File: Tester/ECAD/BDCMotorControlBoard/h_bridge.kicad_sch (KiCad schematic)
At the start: 58 parts, among them Q2 IRLR8726, Q3 IRLR8726, Q4 IRLR8726, Q5 IRLR8726, Q6 BC846, Q7 BC846BPN, Q8 BC846, Q9 BC846, U4 IR2103, U5 INA180A2, U6 IR2103

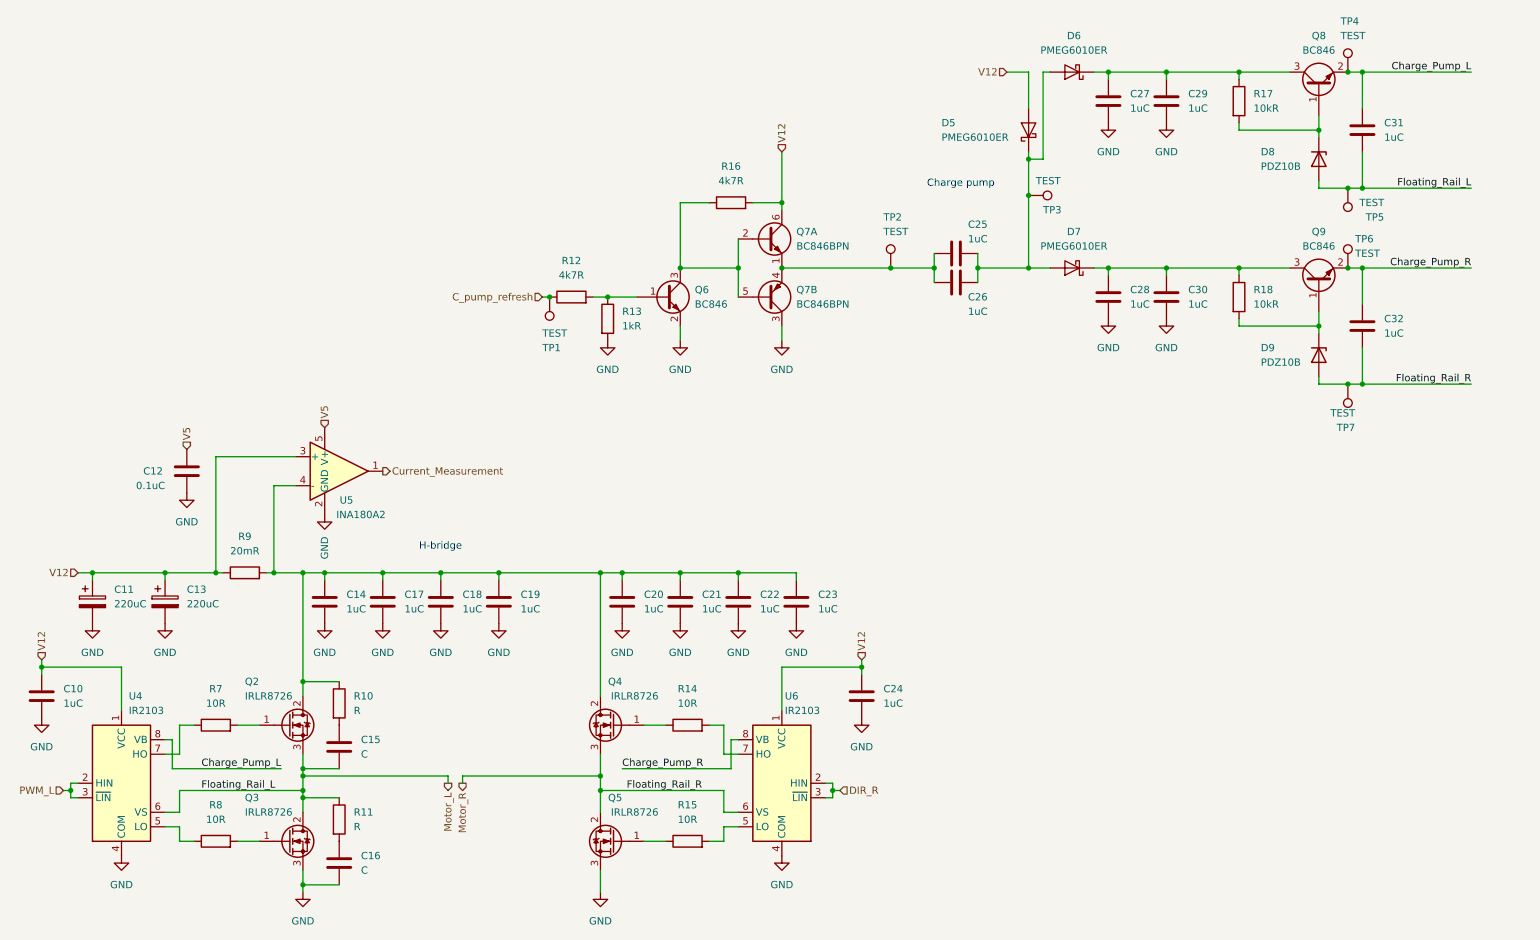
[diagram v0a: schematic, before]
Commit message: Update h_bridge.kicad_sch
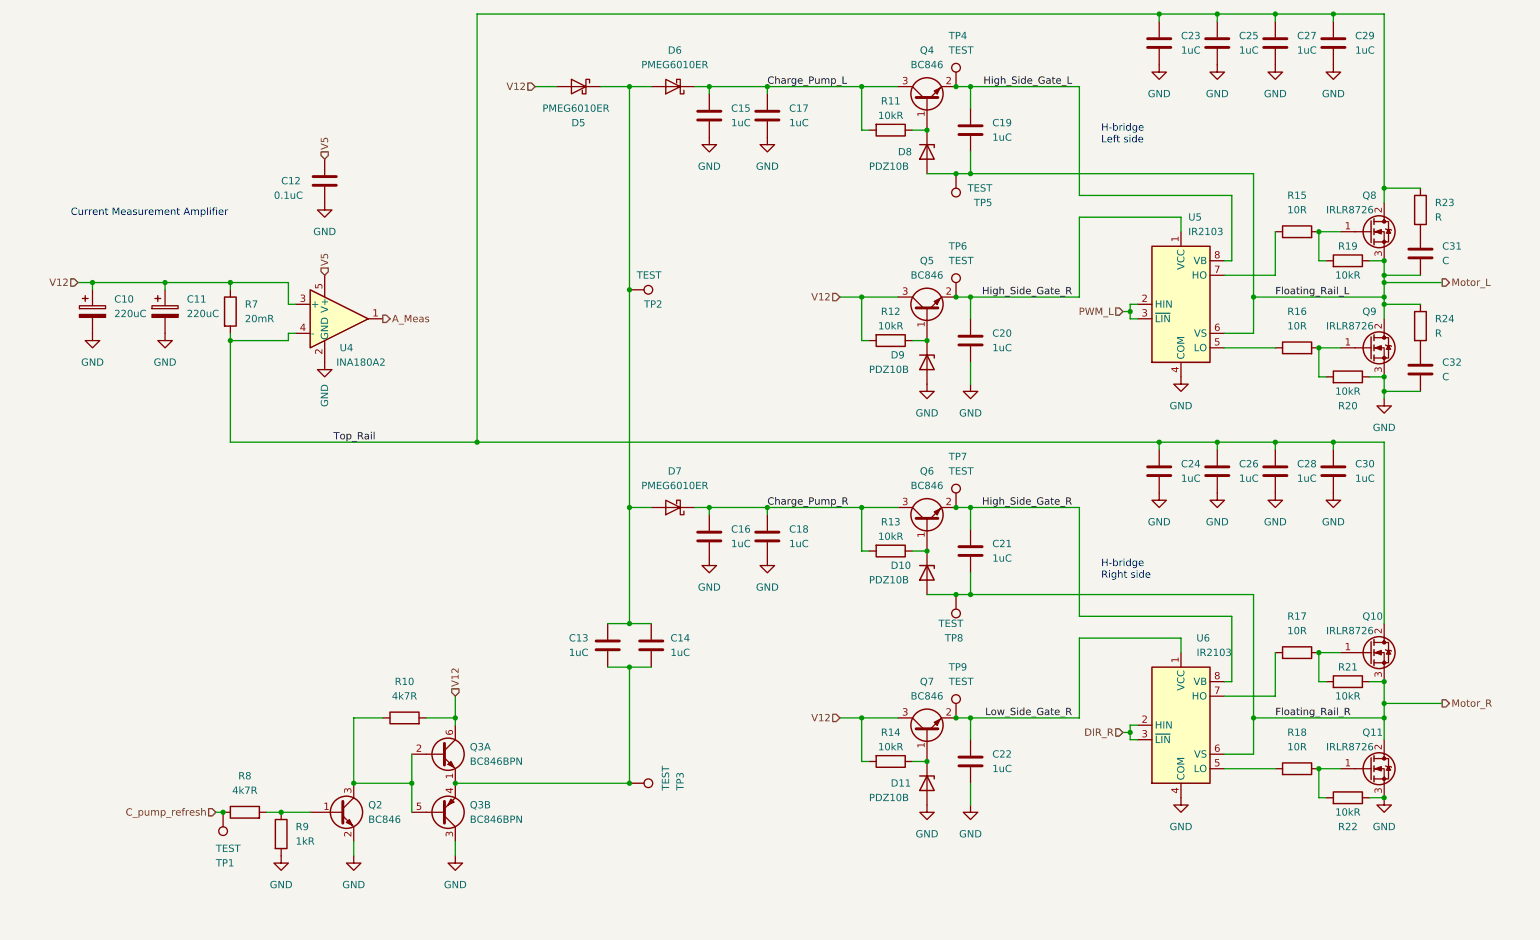
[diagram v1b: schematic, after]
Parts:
- removed C10, C24: 1uC, Capacitor_SMD:C_0805_2012Metric_Pad1.18x1.45mm_HandSolder, symbol Device:C
- added C20, C22: 1uC, Capacitor_SMD:C_0805_2012Metric_Pad1.18x1.45mm_HandSolder, symbol Device:C
- added D11, D9: PDZ10B, Diode_SMD:D_SOD-323_HandSoldering, symbol Device:D_Zener
- added Q5, Q7: BC846, Package_TO_SOT_SMD:SOT-23, symbol Transistor_BJT:BC846
- added R12, R14, R19, R20, R21, R22: 10kR, Resistor_SMD:R_0805_2012Metric_Pad1.20x1.40mm_HandSolder, symbol Device:R
- added TP6, TP9: TEST, TestPoint:TestPoint_Pad_D1.5mm, symbol Connector:TestPoint
- renumbered C11 to C10, C13 to C11, C25 to C13, C26 to C14, C27 to C15, C28 to C16, C29 to C17, C30 to C18, C31 to C19, C32 to C21, C14 to C23, C20 to C24, C17 to C25, C21 to C26, C18 to C27, C22 to C28, C19 to C29, C23 to C30, C15 to C31, C16 to C32, D9 to D10, Q4 to Q10, Q5 to Q11, Q6 to Q2, Q7 to Q3, Q8 to Q4, Q9 to Q6, Q2 to Q8, Q3 to Q9, R16 to R10, R17 to R11, R18 to R13, R7 to R15, R8 to R16, R14 to R17, R15 to R18, R10 to R23, R11 to R24, R9 to R7, R12 to R8, R13 to R9, TP3 to TP2, TP2 to TP3, TP6 to TP7, TP7 to TP8, U5 to U4, U4 to U5
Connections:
- net Charge_Pump_L: now also C15.1, C17.1, D6.1 (K), Q4.3 (C), R11.2; no longer C19.1, Q4.2 (E), TP4.1, U5.8 (VB)
- net Charge_Pump_R: now also C16.1, C18.1, D7.1 (K), Q6.3 (C), R13.2; no longer C21.1, Q6.2 (E), TP7.1, U6.8 (VB)
- net GND: now also C20.2, C22.2, D11.2 (A), D9.2 (A), R20.1, R22.1
- net Motor_L: now also R19.1
- net Motor_R: now also R21.1
- net V12: now also Q5.3 (C), Q7.3 (C), R12.2, R14.2; no longer U5.1 (VCC), U6.1 (VCC)
- net at Q11.1 (G), R18.1: now also R22.2
- net Top_Rail: now reaches C23.1, C24.1, C25.1, C26.1, C27.1, C28.1, C29.1, C30.1, Q10.2 (D), Q8.2 (D), R23.1, R7.2, U4.4 (-)
- net at D8.1 (K), Q4.1 (B): now also R11.1; no longer R11.2
- net at Q9.1 (G), R16.2: now also R20.2
- net at D10.1 (K), Q6.1 (B): now also R13.1; no longer R13.2
- net at Q8.1 (G), R15.2: now also R19.2
- net at Q10.1 (G), R17.1: now also R21.2
- net Current_Measurement renamed A_Meas
- new net: D9.1 (K), Q5.1 (B), R12.1
- new net: D11.1 (K), Q7.1 (B), R14.1
- new net High_Side_Gate_L: C19.1, Q4.2 (E), TP4.1, U5.8 (VB)
- new net High_Side_Gate_R: C20.1, C21.1, Q5.2 (E), Q6.2 (E), TP6.1, TP7.1, U5.1 (VCC), U6.8 (VB)
- new net Low_Side_Gate_R: C22.1, Q7.2 (E), TP9.1, U6.1 (VCC)
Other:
- note added: "Current Measurement Amplifier"
- note added: "H-bridge Left side"
- note added: "H-bridge Right side"
- note removed: "Charge pump"
- note removed: "H-bridge"
- moved on the sheet: C10, C11, C12, C13, C14, C15, C16, C17, C18, C19, C21, C23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

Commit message: Progressed CAD
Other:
- moved on the sheet: C10, C11, C15, C16, C17, C18, C20, C22, C23, C24, C25, C26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

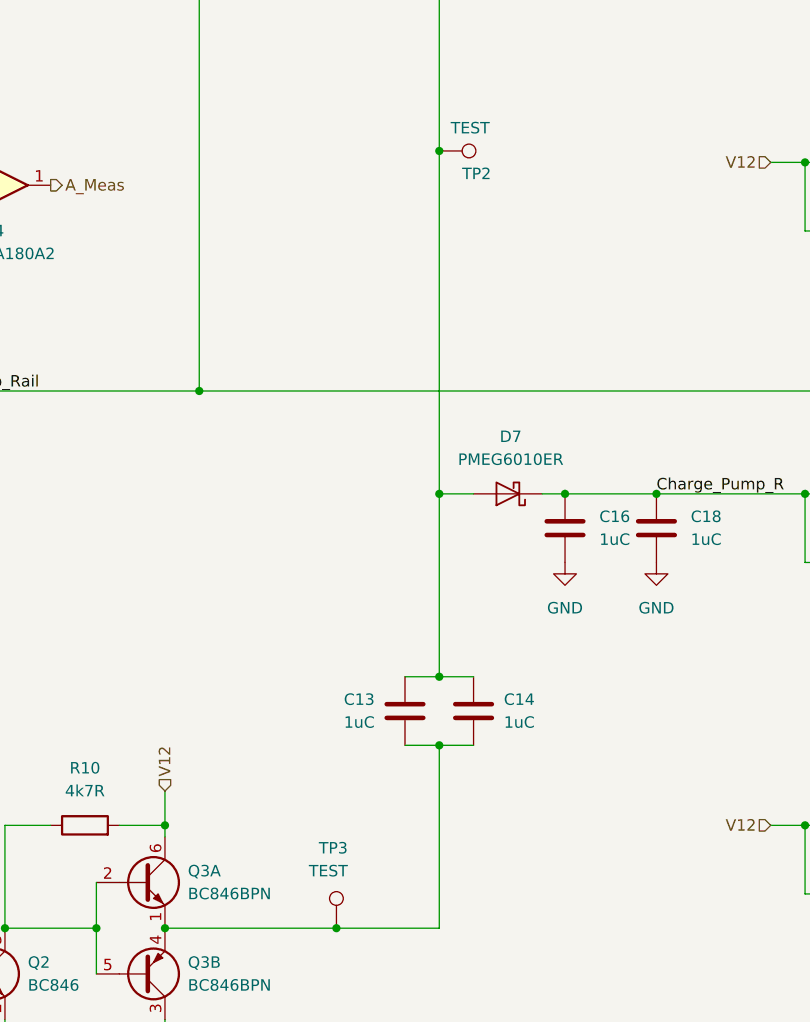
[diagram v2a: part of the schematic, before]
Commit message: Update h_bridge.kicad_sch
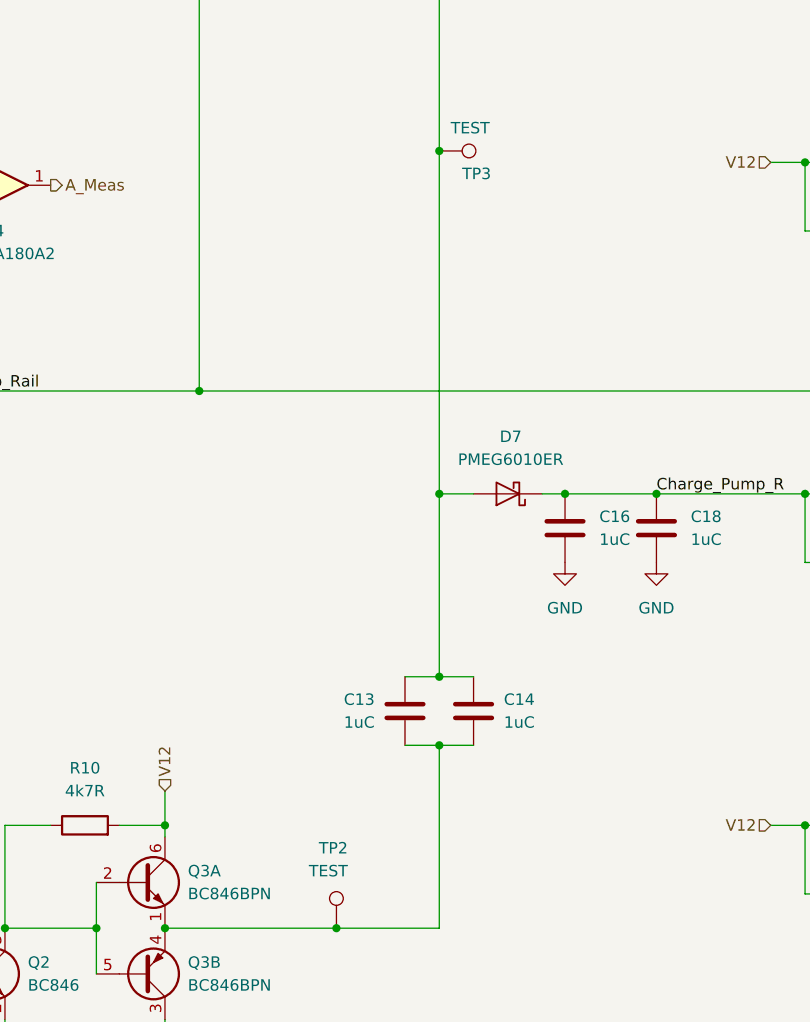
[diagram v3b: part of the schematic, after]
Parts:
- renumbered TP3 to TP2, TP2 to TP3
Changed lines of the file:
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@@
   (symbol (lib_id "Connector:TestPoint") (at 128.27 66.04 270) (mirror x) (unit 1)
     (in_bom yes) (on_board yes)
-    (property "Reference" "TP2" (id 0) (at 130.81 68.58 90)
+    (property "Reference" "TP3" (id 0) (at 130.81 68.58 90)
       (effects (font (size 1.27 1.27)) (justify left))
     )
@@
   (symbol (lib_id "Connector:TestPoint") (at 116.84 152.4 0) (mirror y) (unit 1)
     (in_bom yes) (on_board yes)
-    (property "Reference" "TP3" (id 0) (at 118.11 143.51 0)
+    (property "Reference" "TP2" (id 0) (at 118.11 143.51 0)
       (effects (font (size 1.27 1.27)) (justify left))
     )
@@
   (symbol (lib_id "power:GND") (at 74.93 77.47 0) (unit 1)
     (in_bom yes) (on_board yes) (fields_autoplaced)
-    (property "Reference" "#PWR035" (id 0) (at 74.93 83.82 0)
+    (property "Reference" "#PWR037" (id 0) (at 74.93 83.82 0)
       (effects (font (size 1.27 1.27)) hide)
     )
@@
   (symbol (lib_id "power:GND") (at 80.01 165.1 0) (unit 1)
     (in_bom yes) (on_board yes) (fields_autoplaced)
-    (property "Reference" "#PWR037" (id 0) (at 80.01 171.45 0)
+    (property "Reference" "#PWR038" (id 0) (at 80.01 171.45 0)
       (effects (font (size 1.27 1.27)) hide)
     )
@@
   (symbol (lib_id "power:GND") (at 67.31 165.1 0) (unit 1)
     (in_bom yes) (on_board yes) (fields_autoplaced)
-    (property "Reference" "#PWR036" (id 0) (at 67.31 171.45 0)
+    (property "Reference" "#PWR035" (id 0) (at 67.31 171.45 0)
       (effects (font (size 1.27 1.27)) hide)
     )
@@
   (symbol (lib_id "power:GND") (at 74.93 50.8 0) (unit 1)
     (in_bom yes) (on_board yes) (fields_autoplaced)
-    (property "Reference" "#PWR038" (id 0) (at 74.93 57.15 0)
-      (effects (font (size 1.27 1.27)) hide)
-    )
+    (property "Reference" "#PWR036" (id 0) (at 74.93 57.15 0)
+      (effects (font (size 1.27 1.27)) hide)
+    )

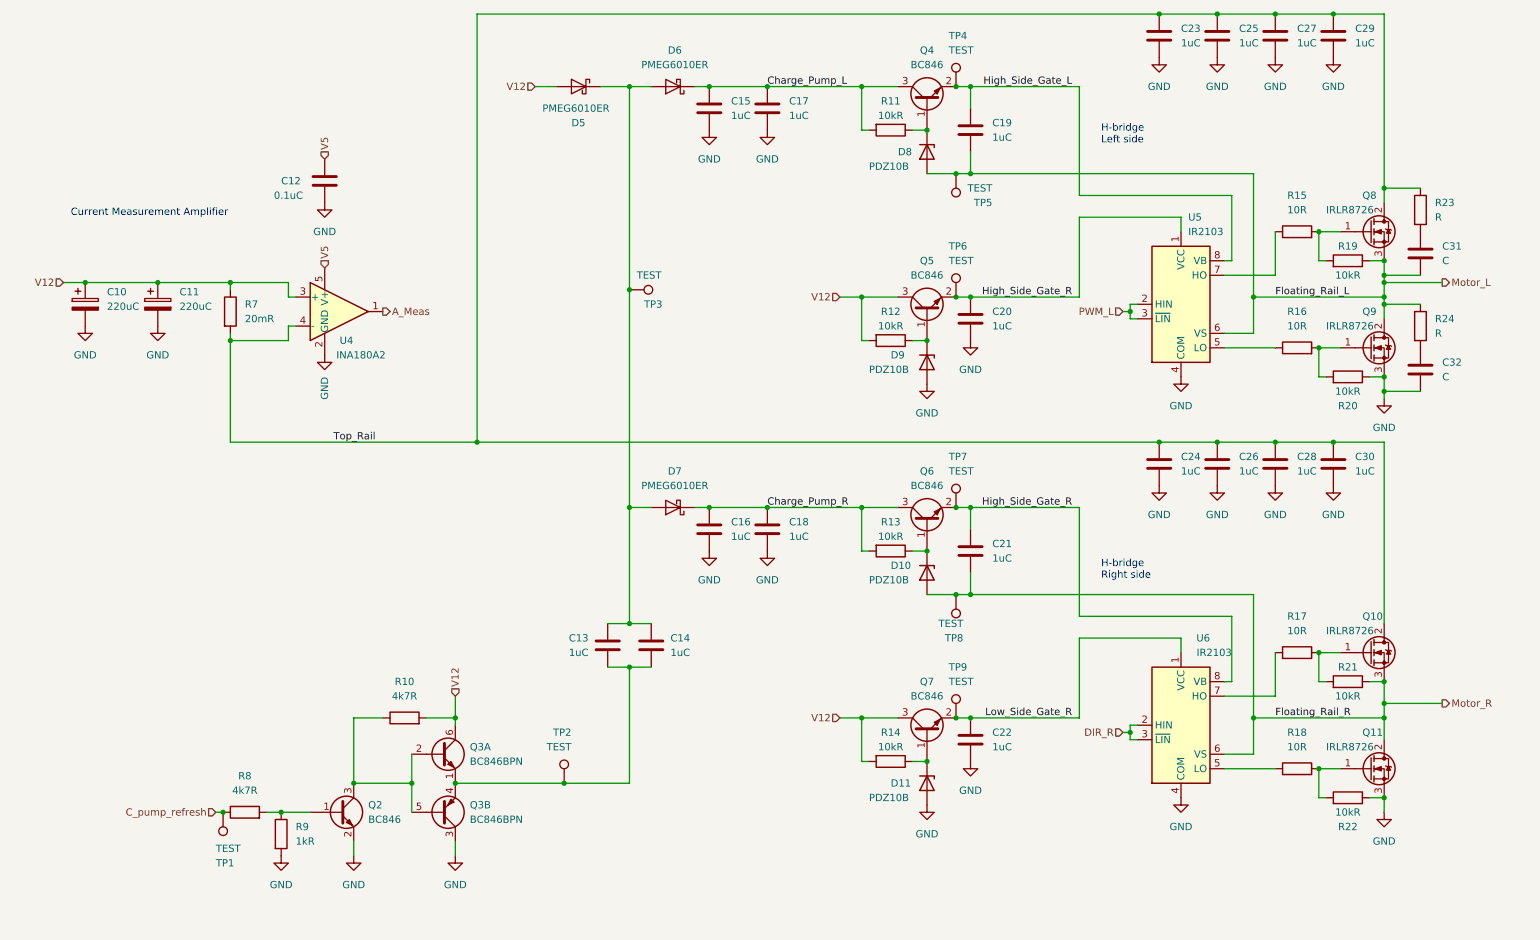
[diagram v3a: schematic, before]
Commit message: Update h_bridge.kicad_sch
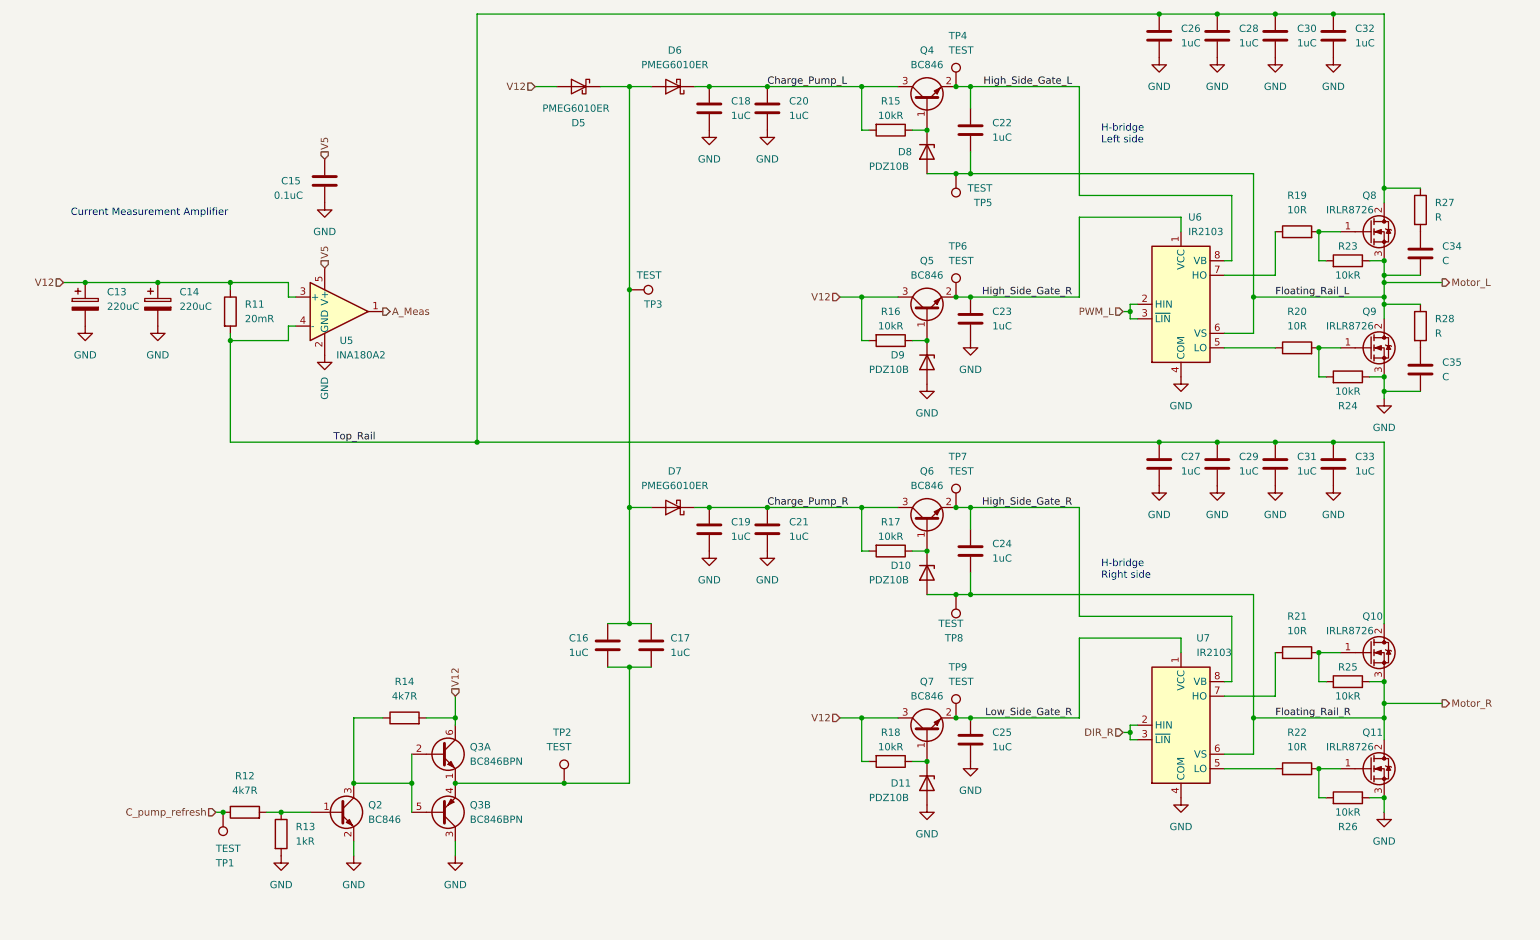
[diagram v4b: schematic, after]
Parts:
- renumbered C10 to C13, C11 to C14, C12 to C15, C13 to C16, C14 to C17, C15 to C18, C16 to C19, C17 to C20, C18 to C21, C19 to C22, C20 to C23, C21 to C24, C22 to C25, C23 to C26, C24 to C27, C25 to C28, C26 to C29, C27 to C30, C28 to C31, C29 to C32, C30 to C33, C31 to C34, C32 to C35, R7 to R11, R8 to R12, R9 to R13, R10 to R14, R11 to R15, R12 to R16, R13 to R17, R14 to R18, R15 to R19, R16 to R20, R17 to R21, R18 to R22, R19 to R23, R20 to R24, R21 to R25, R22 to R26, R23 to R27, R24 to R28, U4 to U5, U5 to U6, U6 to U7
